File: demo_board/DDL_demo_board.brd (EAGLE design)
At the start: 98.7 x 60.3 mm, 36 parts, among them IC1 74LS14N

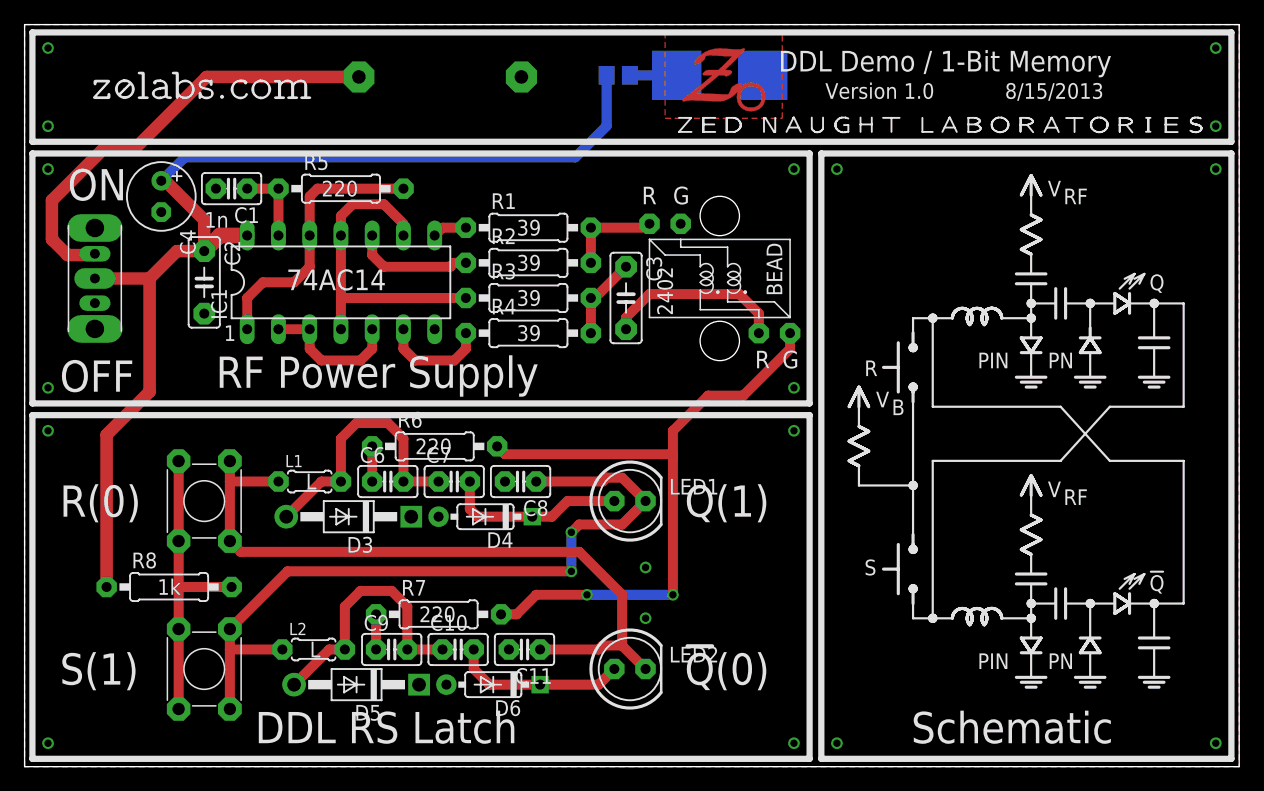
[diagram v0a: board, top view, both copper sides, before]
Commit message: Updated demo board for new inductors * added gerbers to repository * added zip file script
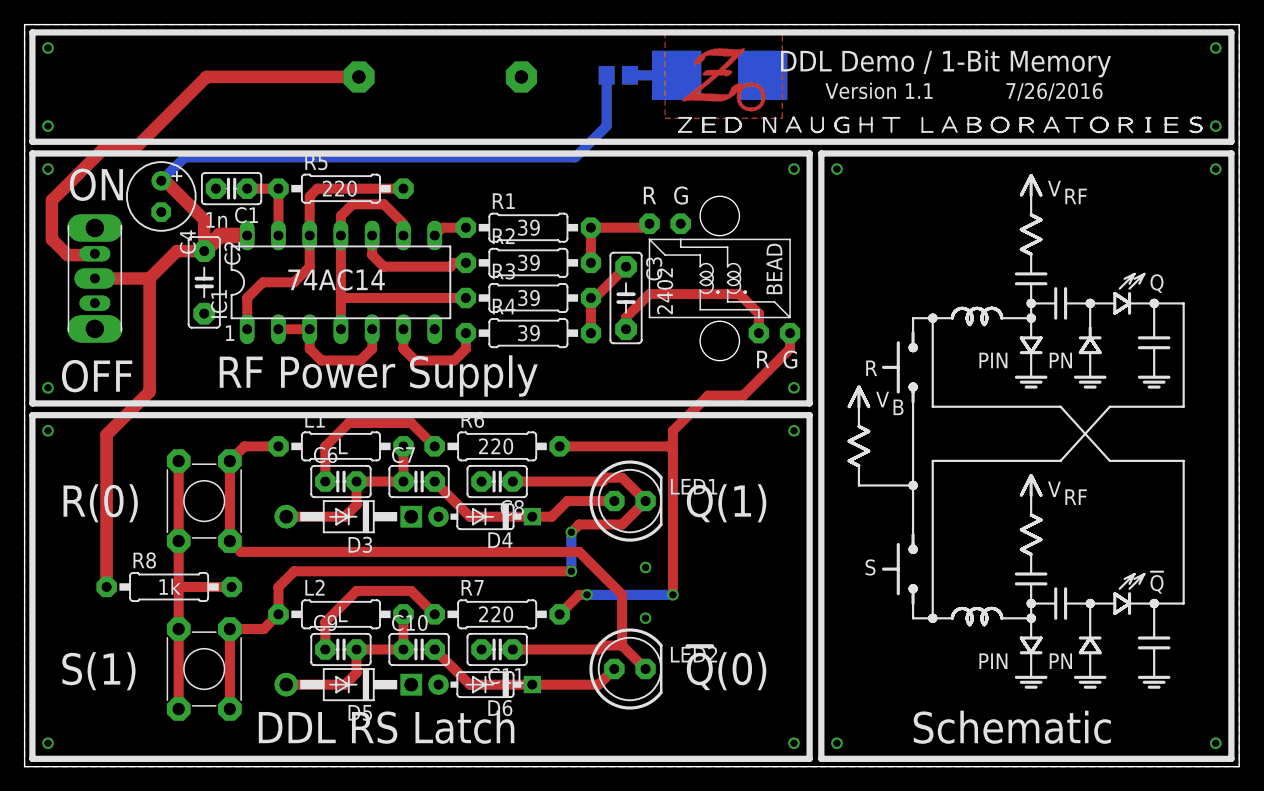
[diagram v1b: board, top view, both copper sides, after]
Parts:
- removed U$31: Z0_LOGO200MIL_NO_Z, z0:Z0_LOGO_NO_Z
- C1: value (none) -> 1n
- C10, C11, C6, C7, C8, C9: value (none) -> 10n
- C2, C3: value (none) -> 100n
- C4: value (none) -> 10u
- L1, L2: value (none) -> 47u; device z0:0204/5 -> z0:0207/10
- LED1, LED2: value (none) -> WP7113SRD/E
- R1, R2, R3, R4: value (none) -> 39
- R5, R6, R7: value (none) -> 220
- R8: value (none) -> 1k
- moved R6 5.08 mm to (38.4, 26.0)
- moved R7 4.76 mm to (38.4, 12.4)
- moved C9 4.13 mm to (25.7, 9.53)
- moved L1 3.82 mm to (25.7, 26.0)
- moved C6 3.81 mm to (25.7, 23.2)
- moved L2 3.62 mm to (25.7, 12.4)
- moved C10 3.17 mm to (32.1, 9.53)
- moved C7 2.86 mm to (32.1, 23.2)
- moved C11 2.22 mm to (38.4, 9.53)
- moved C8 1.91 mm to (38.4, 23.2)
- moved D5 0.64 mm to (26.4, 6.67)
- moved D6 0.63 mm to (37.5, 6.67)
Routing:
- net N$6: track 2.86 -> 13.3 mm
- net N$16: track 2.86 -> 13.0 mm
- net VRF: track 56.1 -> 46.1 mm
- net N$11: track 21.6 -> 14.7 mm
- net N$18: track 21.3 -> 14.7 mm
- net N$22: track 57.8 -> 60.5 mm
- net N$19: track 14.1 -> 16.3 mm
- net N$2: track 14.8 -> 16.3 mm
- net N$24: track 60.5 -> 59.5 mm
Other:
- board text added: "7/26/2016"
- board text added: "Serial V1.1-"
- board text added: "Version 1.1"
- board text removed: "8/15/2013"
- board text removed: "Serial V1.0-"
- board text removed: "Version 1.0"
